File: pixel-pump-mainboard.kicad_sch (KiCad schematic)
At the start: 121 parts, among them J1 JST NC Valve, J10 BM10B-SRSS-TB(LF)(SN), J11 UART/SWD DNP, J12 TYPE-C-31-M-12, J2 JST NO Valve, J3 6P4C, J4 JST 3 Way Valve, J5 Jack-DC 12V, J6 Power Sw, J7 I2C, J8 SPI, J9 BM04B-SRSS-TBT(LF)(SN), Q1 BSS138, Q2 BSS138, Q3 BSS138, Q4 STN4NF20L, Q5 BSS138, SW1 BOOTSEL, U1 LD1117S33TR, U2 TPS62112RSAR, U3 W25Q128JVS, U4 RP2040, Y1 ABMM2-12.000MHZ-E2-T

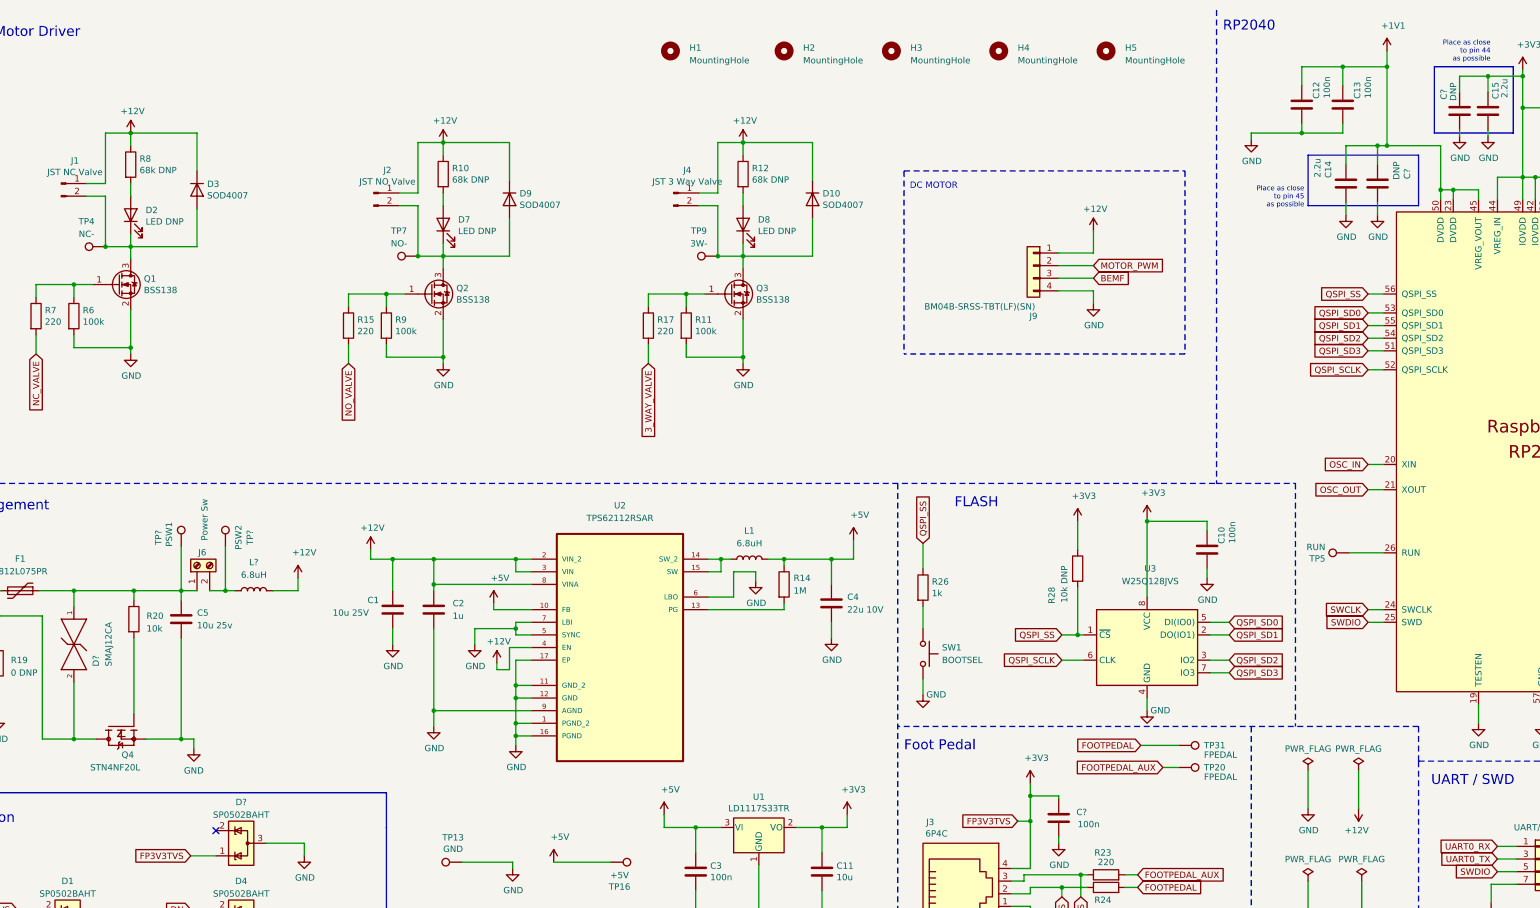
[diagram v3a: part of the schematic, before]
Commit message: ERC & Assigned footprints
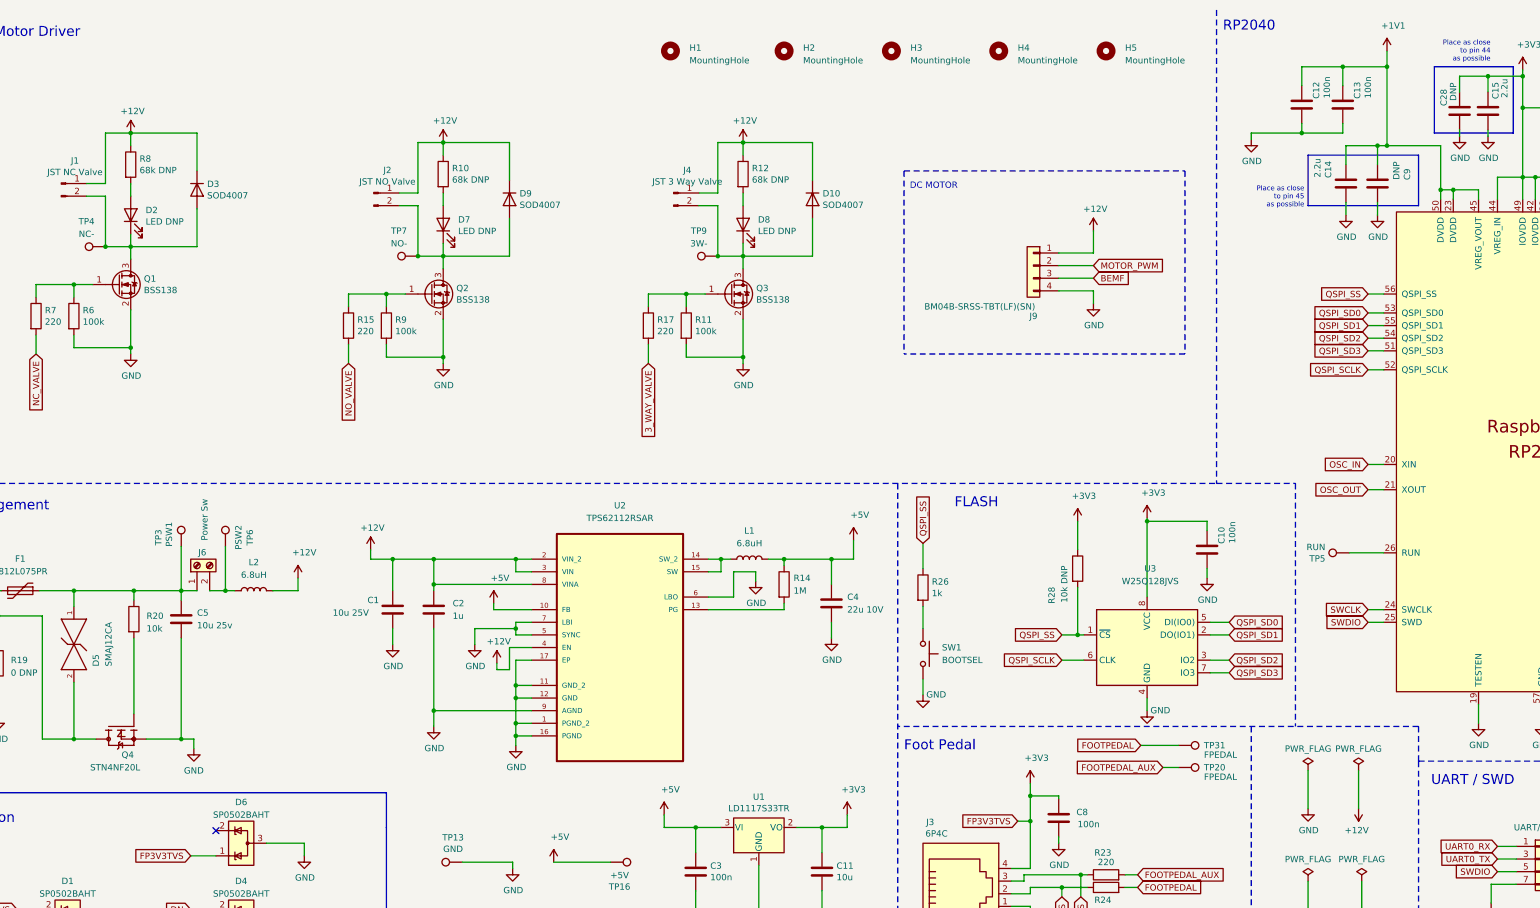
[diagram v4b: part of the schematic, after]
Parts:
- D5: renamed from D?; footprint Littelfuse_Inc-SMAJ-CA-0-0-* -> Diode_SMD:D_SMA
- gave numbers to parts that had none: 7
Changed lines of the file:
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@@
   (symbol (lib_id "SMAJ12CA:SMAJ12CA") (at 46.99 130.175 270) (unit 1)
     (in_bom yes) (on_board yes)
-    (property "Reference" "D?" (id 0) (at 51.435 144.7801 0)
+    (property "Reference" "D5" (id 0) (at 51.435 144.7801 0)
       (effects (font (size 1.27 1.27)) (justify right))
     )
@@
       (effects (font (size 1.27 1.27)) (justify right))
     )
-    (property "Footprint" "Littelfuse_Inc-SMAJ-CA-0-0-*" (id 2) (at 57.15 130.175 0)
+    (property "Footprint" "Diode_SMD:D_SMA" (id 2) (at 57.15 130.175 0)
       (effects (font (size 1.27 1.27)) (justify left) hide)
     )
@@
   (symbol (lib_id "power:GND") (at 245.11 180.34 0) (unit 1)
     (in_bom yes) (on_board yes)
-    (property "Reference" "#PWR?" (id 0) (at 245.11 186.69 0)
+    (property "Reference" "#PWR051" (id 0) (at 245.11 186.69 0)
       (effects (font (size 1.27 1.27)) hide)
     )
@@
   (symbol (lib_id "Device:C") (at 245.11 175.26 180) (unit 1)
     (in_bom yes) (on_board yes)
-    (property "Reference" "C?" (id 0) (at 248.666 174.0916 0)
+    (property "Reference" "C8" (id 0) (at 248.666 174.0916 0)
       (effects (font (size 1.27 1.27)) (justify right))
     )
@@
   (symbol (lib_id "power:GND") (at 93.345 182.88 0) (unit 1)
     (in_bom yes) (on_board yes)
-    (property "Reference" "#PWR?" (id 0) (at 93.345 189.23 0)
+    (property "Reference" "#PWR047" (id 0) (at 93.345 189.23 0)
       (effects (font (size 1.27 1.27)) hide)
     )
@@
   (symbol (lib_id "Power_Protection:SP0502BAHT") (at 80.645 180.34 90) (unit 1)
     (in_bom yes) (on_board yes) (fields_autoplaced)
-    (property "Reference" "D?" (id 0) (at 80.645 172.085 90))
+    (property "Reference" "D6" (id 0) (at 80.645 172.085 90))
     (property "Value" "SP0502BAHT" (id 1) (at 80.645 174.625 90))
     (property "Footprint" "Package_TO_SOT_SMD:SOT-23" (id 2) (at 81.915 174.625 0)
@@
   (symbol (lib_id "power:GND") (at 309.245 53.975 0) (unit 1)
     (in_bom yes) (on_board yes)
-    (property "Reference" "#PWR?" (id 0) (at 309.245 60.325 0)
+    (property "Reference" "#PWR052" (id 0) (at 309.245 60.325 0)
       (effects (font (size 1.27 1.27)) hide)
     )
@@
   (symbol (lib_id "Connector:TestPoint") (at 77.47 120.65 0) (unit 1)
     (in_bom yes) (on_board yes)
-    (property "Reference" "TP?" (id 0) (at 82.423 118.8212 90))
+    (property "Reference" "TP6" (id 0) (at 82.423 118.8212 90))
     (property "Value" "PSW2" (id 1) (at 80.112 118.821 90))
     (property "Footprint" "TestPoint:TestPoint_Pad_D2.0mm" (id 2) (at 82.55 120.65 0)
@@
   (symbol (lib_id "Device:L") (at 83.185 129.54 90) (unit 1)
     (in_bom yes) (on_board yes) (fields_autoplaced)
-    (property "Reference" "L?" (id 0) (at 83.185 123.825 90))
+    (property "Reference" "L2" (id 0) (at 83.185 123.825 90))
     (property "Value" "6.8uH" (id 1) (at 83.185 126.365 90))
     (property "Footprint" "Inductor_SMD:L_TDK_SLF7032" (id 2) (at 83.185 129.54 0)
@@
   (symbol (lib_id "Device:C") (at 325.755 33.02 0) (unit 1)
     (in_bom yes) (on_board yes)
-    (property "Reference" "C?" (id 0) (at 322.58 28.6004 90)
+    (property "Reference" "C28" (id 0) (at 322.58 28.6004 90)
       (effects (font (size 1.27 1.27)) (justify right))
     )
@@
   (symbol (lib_id "Connector:TestPoint") (at 68.58 120.65 0) (unit 1)
     (in_bom yes) (on_board yes)
-    (property "Reference" "TP?" (id 0) (at 64.008 118.8212 90))
+    (property "Reference" "TP3" (id 0) (at 64.008 118.8212 90))
     (property "Value" "PSW1" (id 1) (at 66.142 118.186 90))
     (property "Footprint" "TestPoint:TestPoint_Pad_D2.0mm" (id 2) (at 73.66 120.65 0)
@@
   (symbol (lib_id "power:GND") (at 325.755 38.1 0) (unit 1)
     (in_bom yes) (on_board yes)
-    (property "Reference" "#PWR?" (id 0) (at 325.755 44.45 0)
+    (property "Reference" "#PWR053" (id 0) (at 325.755 44.45 0)
       (effects (font (size 1.27 1.27)) hide)
     )
@@
   (symbol (lib_id "Device:C") (at 309.245 47.625 0) (unit 1)
     (in_bom yes) (on_board yes)
-    (property "Reference" "C?" (id 0) (at 315.214 44.6024 90)
+    (property "Reference" "C9" (id 0) (at 315.214 44.6024 90)
       (effects (font (size 1.27 1.27)) (justify right))
     )
@@
       (reference "#PWR046") (unit 1) (value "GND") (footprint "")
     )
+    (path "/656263cd-a553-4d5e-94a2-ec750e36dd23"
+      (reference "#PWR047") (unit 1) (value "GND") (footprint "")
+    )
     (path "/c91c65e0-b015-48ec-810e-87c47c31276e"
       (reference "#PWR048") (unit 1) (value "GND") (footprint "")
@@
       (reference "#PWR050") (unit 1) (value "+5V") (footprint "")
     )
+    (path "/04fbeb4d-1f5e-4cc1-a1c6-06b82e55fec8"
+      (reference "#PWR051") (unit 1) (value "GND") (footprint "")
+    )
+    (path "/71bbef32-3387-4c77-b0ac-94baa11e2466"
+      (reference "#PWR052") (unit 1) (value "GND") (footprint "")
+    )
+    (path "/edc12b9d-a4c3-4954-9a48-70bcad896f7a"
+      (reference "#PWR053") (unit 1) (value "GND") (footprint "")
+    )
     (path "/51fb0a17-77ea-4f1c-b1a9-892942582436"
       (reference "#PWR0101") (unit 1) (value "+5V") (footprint "")
@@
       (reference "#PWR0177") (unit 1) (value "+12V") (footprint "")
     )
-    (path "/04fbeb4d-1f5e-4cc1-a1c6-06b82e55fec8"
-      (reference "#PWR?") (unit 1) (value "GND") (footprint "")
-    )
-    (path "/656263cd-a553-4d5e-94a2-ec750e36dd23"
-      (reference "#PWR?") (unit 1) (value "GND") (footprint "")
-    )
-    (path "/71bbef32-3387-4c77-b0ac-94baa11e2466"
-      (reference "#PWR?") (unit 1) (value "GND") (footprint "")
-    )
-    (path "/edc12b9d-a4c3-4954-9a48-70bcad896f7a"
-      (reference "#PWR?") (unit 1) (value "GND") (footprint "")
-    )
     (path "/f2f8bd37-909b-41a4-8113-25e4c56a139c"
       (reference "C1") (unit 1) (value "10u 25V") (footprint "Capacitor_SMD:C_1210_3225Metric")
@@
       (reference "C7") (unit 1) (value "27p") (footprint "Capacitor_SMD:C_0603_1608Metric")
     )
+    (path "/0c9f9409-df68-405b-9b9a-0a3c681ff164"
+      (reference "C8") (unit 1) (value "100n") (footprint "Capacitor_SMD:C_0603_1608Metric")
+    )
+    (path "/fcce3af6-bd65-47bf-b11f-30353ee394c6"
+      (reference "C9") (unit 1) (value "DNP") (footprint "Capacitor_SMD:C_0402_1005Metric")
+    )
     (path "/a96ebdb9-5820-4d66-9f7d-3d99d74f050a"
       (reference "C10") (unit 1) (value "100n") (footprint "Capacitor_SMD:C_0402_1005Metric")
@@
       (reference "C27") (unit 1) (value "100n") (footprint "Capacitor_SMD:C_0603_1608Metric")
     )
-    (path "/0c9f9409-df68-405b-9b9a-0a3c681ff164"
-      (reference "C?") (unit 1) (value "100n") (footprint "Capacitor_SMD:C_0603_1608Metric")
-    )
     (path "/d2052ab4-d2a1-4ba1-8e79-e53b1f2a4f63"
-      (reference "C?") (unit 1) (value "DNP") (footprint "Capacitor_SMD:C_0402_1005Metric")
-    )
-    (path "/fcce3af6-bd65-47bf-b11f-30353ee394c6"
-      (reference "C?") (unit 1) (value "DNP") (footprint "Capacitor_SMD:C_0402_1005Metric")
+      (reference "C28") (unit 1) (value "DNP") (footprint "Capacitor_SMD:C_0402_1005Metric")
     )
     (path "/400e7f02-3fa9-441b-9158-d4a9ac83b942"
@@
       (reference "D4") (unit 1) (value "SP0502BAHT") (footprint "Package_TO_SOT_SMD:SOT-23")
     )
+    (path "/04d46d44-29f0-41e2-b9c2-faca40bb6170"
+      (reference "D5") (unit 1) (value "SMAJ12CA") (footprint "Diode_SMD:D_SMA")
+    )
+    (path "/6a9588f5-5a62-4bc2-9606-c8cac96c59f6"
+      (reference "D6") (unit 1) (value "SP0502BAHT") (footprint "Package_TO_SOT_SMD:SOT-23")
+    )
     (path "/00000000-0000-0000-0000-0000605beb31"
       (reference "D7") (unit 1) (value "LED DNP") (footprint "LED_SMD:LED_0603_1608Metric")
@@
       (reference "D10") (unit 1) (value "SOD4007") (footprint "Diode_SMD:D_SOD-123F")
     )
-    (path "/04d46d44-29f0-41e2-b9c2-faca40bb6170"
-      (reference "D?") (unit 1) (value "SMAJ12CA") (footprint "Littelfuse_Inc-SMAJ-CA-0-0-*")
-    )
-    (path "/6a9588f5-5a62-4bc2-9606-c8cac96c59f6"
-      (reference "D?") (unit 1) (value "SP0502BAHT") (footprint "Package_TO_SOT_SMD:SOT-23")
-    )
     (path "/61625a32-c238-40ad-b2a9-98b507a4a82c"
       (reference "F1") (unit 1) (value "1812L075PR") (footprint "Fuse:Fuse_1812_4532Metric")
@@
     )
     (path "/9f1122b9-9748-4ccf-aa2f-d98f75196857"
-      (reference "L?") (unit 1) (value "6.8uH") (footprint "Inductor_SMD:L_TDK_SLF7032")
+      (reference "L2") (unit 1) (value "6.8uH") (footprint "Inductor_SMD:L_TDK_SLF7032")
     )
     (path "/00000000-0000-0000-0000-0000604afb22"
@@
       (reference "TP2") (unit 1) (value "USB D-") (footprint "TestPoint:TestPoint_Pad_D2.0mm")
     )
+    (path "/eaf4e827-48c7-474b-9b97-75c6139eb8f0"
+      (reference "TP3") (unit 1) (value "PSW1") (footprint "TestPoint:TestPoint_Pad_D2.0mm")
+    )
     (path "/00000000-0000-0000-0000-0000615f04a2"
       (reference "TP4") (unit 1) (value "NC-") (footprint "TestPoint:TestPoint_Pad_D2.0mm")
@@
       (reference "TP5") (unit 1) (value "RUN") (footprint "TestPoint:TestPoint_Pad_D2.0mm")
     )
+    (path "/7e6da121-6b6e-4747-b19a-096c4bd1260a"
+      (reference "TP6") (unit 1) (value "PSW2") (footprint "TestPoint:TestPoint_Pad_D2.0mm")
+    )
     (path "/00000000-0000-0000-0000-0000615f0e5c"
       (reference "TP7") (unit 1) (value "NO-") (footprint "TestPoint:TestPoint_Pad_D2.0mm")
@@
       (reference "TP31") (unit 1) (value "FPEDAL") (footprint "TestPoint:TestPoint_Pad_D2.0mm")
     )
-    (path "/7e6da121-6b6e-4747-b19a-096c4bd1260a"
-      (reference "TP?") (unit 1) (value "PSW2") (footprint "TestPoint:TestPoint_Pad_D2.0mm")
-    )
-    (path "/eaf4e827-48c7-474b-9b97-75c6139eb8f0"
-      (reference "TP?") (unit 1) (value "PSW1") (footprint "TestPoint:TestPoint_Pad_D2.0mm")
-    )
     (path "/00000000-0000-0000-0000-00005fe07207"
